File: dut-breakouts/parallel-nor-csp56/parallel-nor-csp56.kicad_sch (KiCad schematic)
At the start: 14 parts, among them J1 CONN_DUMPTRUCK_DEVICE, M1 LOGO, M2 LOGO, M3 LOGO, M4 LOGO, U1 MX29GL512FLXGI, U2 M24C02-RMC6TG

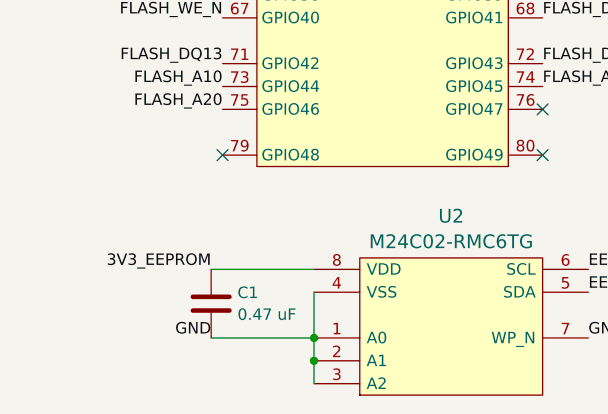
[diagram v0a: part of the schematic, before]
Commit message: parallel-nor-csp56: fixed eeprom address
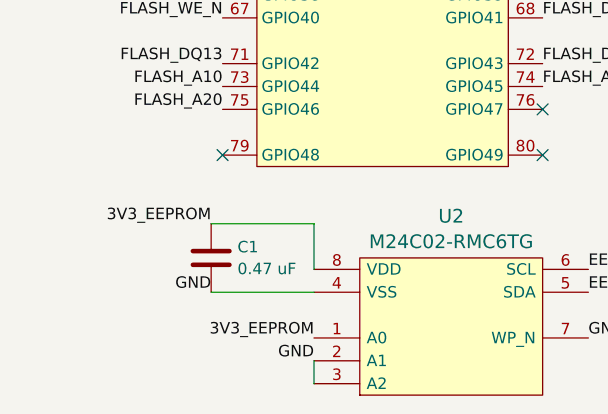
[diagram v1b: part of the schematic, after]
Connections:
- net 3V3_EEPROM: now also U2.1 (A0)
- net GND: no longer U2.1 (A0)
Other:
- moved on the sheet: C1
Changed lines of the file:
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@@
 	)
 	(junction
-		(at 44.45 186.69)
-		(diameter 0)
-		(color 0 0 0 0)
-	)
-	(junction
 		(at 34.29 62.23)
 		(diameter 0)
@@
 	)
 	(junction
-		(at 44.45 189.23)
-		(diameter 0)
-		(color 0 0 0 0)
-	)
-	(junction
 		(at 67.31 49.53)
 		(diameter 0)
@@
 	(wire
 		(pts
-			(xy 33.02 77.47) (xy 34.29 77.47)
+			(xy 44.45 173.99) (xy 44.45 179.07)
 		)
 		(stroke
@@
 	(wire
 		(pts
-			(xy 34.29 62.23) (xy 34.29 64.77)
+			(xy 33.02 77.47) (xy 34.29 77.47)
 		)
 		(stroke
@@
 	(wire
 		(pts
-			(xy 44.45 189.23) (xy 44.45 191.77)
+			(xy 34.29 62.23) (xy 34.29 64.77)
 		)
 		(stroke
@@
 	(wire
 		(pts
-			(xy 67.31 46.99) (xy 67.31 49.53)
+			(xy 44.45 189.23) (xy 44.45 191.77)
 		)
 		(stroke
@@
 	(wire
 		(pts
-			(xy 201.93 97.79) (xy 223.52 97.79)
+			(xy 67.31 46.99) (xy 67.31 49.53)
 		)
 		(stroke
@@
 	(wire
 		(pts
-			(xy 67.31 57.15) (xy 67.31 59.69)
+			(xy 201.93 97.79) (xy 223.52 97.79)
 		)
 		(stroke
@@
 	(wire
 		(pts
-			(xy 34.29 57.15) (xy 34.29 59.69)
+			(xy 33.02 173.99) (xy 44.45 173.99)
 		)
 		(stroke
@@
 	(wire
 		(pts
-			(xy 67.31 59.69) (xy 67.31 62.23)
+			(xy 67.31 57.15) (xy 67.31 59.69)
 		)
 		(stroke
@@
 	(wire
 		(pts
-			(xy 67.31 41.91) (xy 67.31 44.45)
+			(xy 34.29 57.15) (xy 34.29 59.69)
 		)
 		(stroke
@@
 	(wire
 		(pts
-			(xy 176.53 153.67) (xy 189.23 153.67)
+			(xy 67.31 59.69) (xy 67.31 62.23)
 		)
 		(stroke
@@
 	(wire
 		(pts
-			(xy 33.02 179.07) (xy 44.45 179.07)
+			(xy 67.31 41.91) (xy 67.31 44.45)
 		)
 		(stroke
@@
 	(wire
 		(pts
-			(xy 44.45 181.61) (xy 44.45 186.69)
+			(xy 176.53 153.67) (xy 189.23 153.67)
 		)
 		(stroke
@@
 	(wire
 		(pts
-			(xy 33.02 186.69) (xy 44.45 186.69)
-		)
-		(stroke
-			(width 0)
-			(type default)
-		)
-	)
-	(wire
-		(pts
 			(xy 67.31 54.61) (xy 67.31 57.15)
 		)
@@
 	(wire
 		(pts
-			(xy 34.29 52.07) (xy 34.29 54.61)
+			(xy 33.02 181.61) (xy 44.45 181.61)
 		)
 		(stroke
@@
 	(wire
 		(pts
-			(xy 44.45 186.69) (xy 44.45 189.23)
+			(xy 34.29 52.07) (xy 34.29 54.61)
 		)
 		(stroke
@@
 	)
 	(label "3V3_EEPROM"
-		(at 33.02 179.07 180)
+		(at 33.02 173.99 180)
 		(fields_autoplaced yes)
 		(effects
@@
 		)
 	)
+	(label "3V3_EEPROM"
+		(at 44.45 186.69 180)
+		(fields_autoplaced yes)
+		(effects
+			(font
+				(size 1.27 1.27)
+			)
+			(justify right bottom)
+		)
+	)
 	(label "FLASH_A3"
 		(at 69.85 128.27 0)
@@
 		)
 	)
+	(label "GND"
+		(at 44.45 189.23 180)
+		(fields_autoplaced yes)
+		(effects
+			(font
+				(size 1.27 1.27)
+			)
+			(justify right bottom)
+		)
+	)
 	(label "FLASH_A9"
 		(at 146.05 49.53 180)
@@
 	)
 	(label "GND"
-		(at 33.02 186.69 180)
+		(at 33.02 181.61 180)
 		(fields_autoplaced yes)
 		(effects
@@
 	(symbol
 		(lib_id "device:C")
-		(at 33.02 182.88 0)
+		(at 33.02 177.8 0)
 		(unit 1)
 		(exclude_from_sim no)
@@
 		(fields_autoplaced yes)
 		(property "Reference" "C1"
-			(at 35.941 181.6678 0)
+			(at 35.941 176.5878 0)
 			(effects
 				(font
@@
 		)
 		(property "Value" "0.47 uF"
-			(at 35.941 184.0921 0)
+			(at 35.941 179.0121 0)
 			(effects
 				(font
@@
 		)
 		(property "Footprint" "azonenberg_pcb:EIA_0402_CAP_NOSILK"
-			(at 33.9852 186.69 0)
+			(at 33.9852 181.61 0)
 			(effects
 				(font
@@
 		)
 		(property "Datasheet" ""
-			(at 33.02 182.88 0)
+			(at 33.02 177.8 0)
 			(effects
 				(font
@@
 		)
 		(property "Description" "Unpolarized capacitor"
-			(at 33.02 182.88 0)
+			(at 33.02 177.8 0)
 			(effects
 				(font
